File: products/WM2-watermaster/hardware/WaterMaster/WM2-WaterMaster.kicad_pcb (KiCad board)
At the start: 2 copper layers, 97.4 x 99.1 mm, 109 parts, among them J1 Flow_CONN, J12 Conn_01x04_Pin, J13 Conn_01x03_Pin, J2 Conn_Coaxial_Small, J3 PWR_CONN, J4 Conn_IN, J5 Conn_01x03_Pin, J7 Conn_RLY_EXTENDER, K1 Cube_Relay, K2 Cube_Relay, K3 Cube_Relay, K4 Cube_Relay, K5 Cube_Relay, K6 Cube_Relay, U1 ULN2003, U10 DS1307Z+, U13 AMS1117-5.0, U2 74HC595, U3 MT3608, U4 DS3231M, U5 ESP32 30 Pin CP2102 Developme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, U7 ISC-SX1262-B, U8 AP2112K-3.3, U9 74HC595, Y1 Crystal

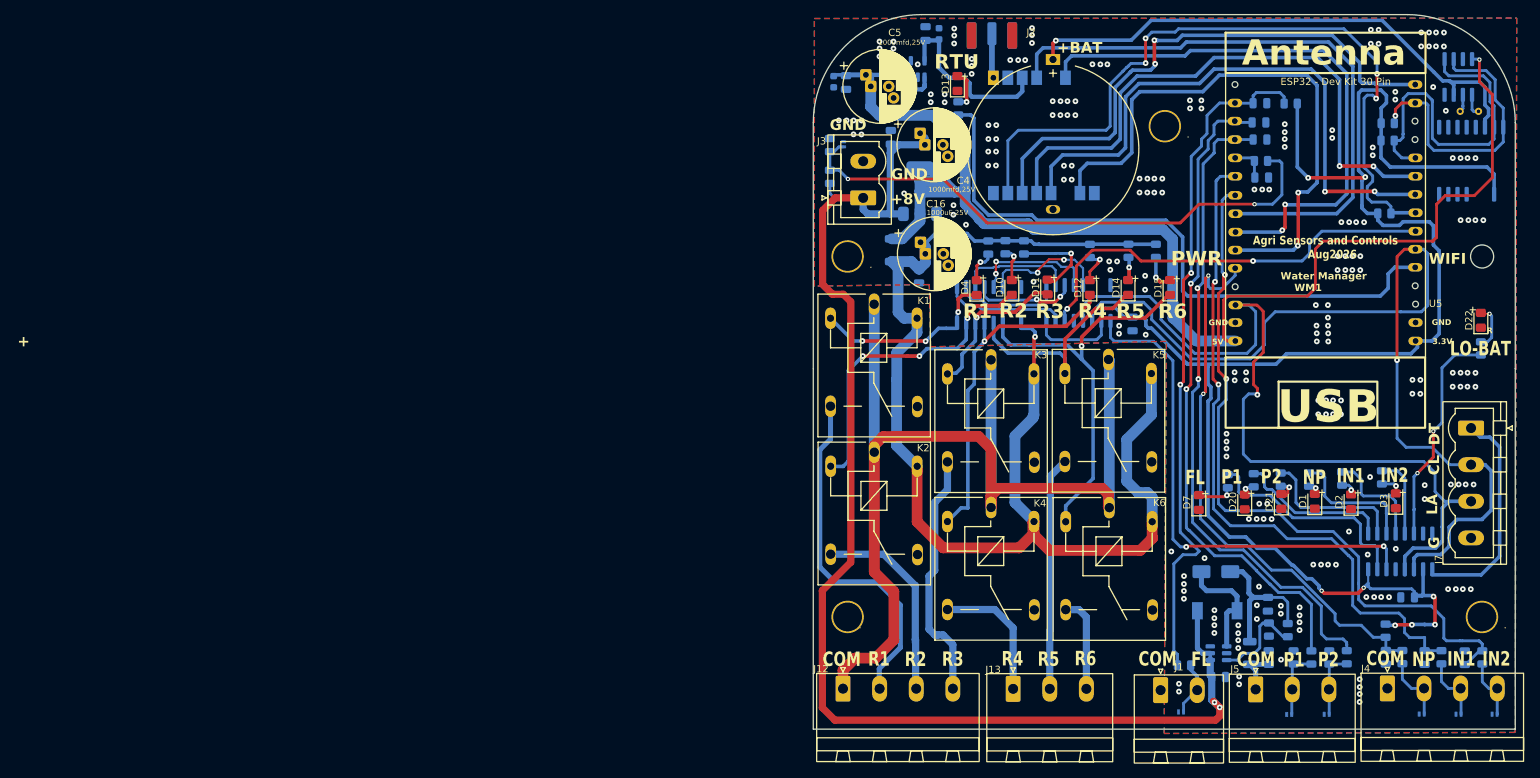
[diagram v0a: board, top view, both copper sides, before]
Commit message: Workshop labs page at /workshop, GPSIOAM workshop materials, pending WIP
- agrisense-webapp: public, no-login /workshop route (middleware allowlist +
  next.config.ts rewrite) serving the student labs page from public/workshop
- docs/workshops/gpsioam-2026: 4 Wokwi-ready ESP32 labs + Lab 4 reference
  solution, labs page template and build_site.py
- Pending work committed as-is: WM2 SolarNode/WaterMaster KiCad, WPC Pump
  Node Gerbers, FG1 flash tools, marketing video projects
- .gitignore: Next.js cache, *.tsbuildinfo, KiCad *.lck, .claude/settings.local.json;
  stop tracking .next/cache

Co-Authored-By: Claude Opus 5.5 <noreply@anthropic.com>
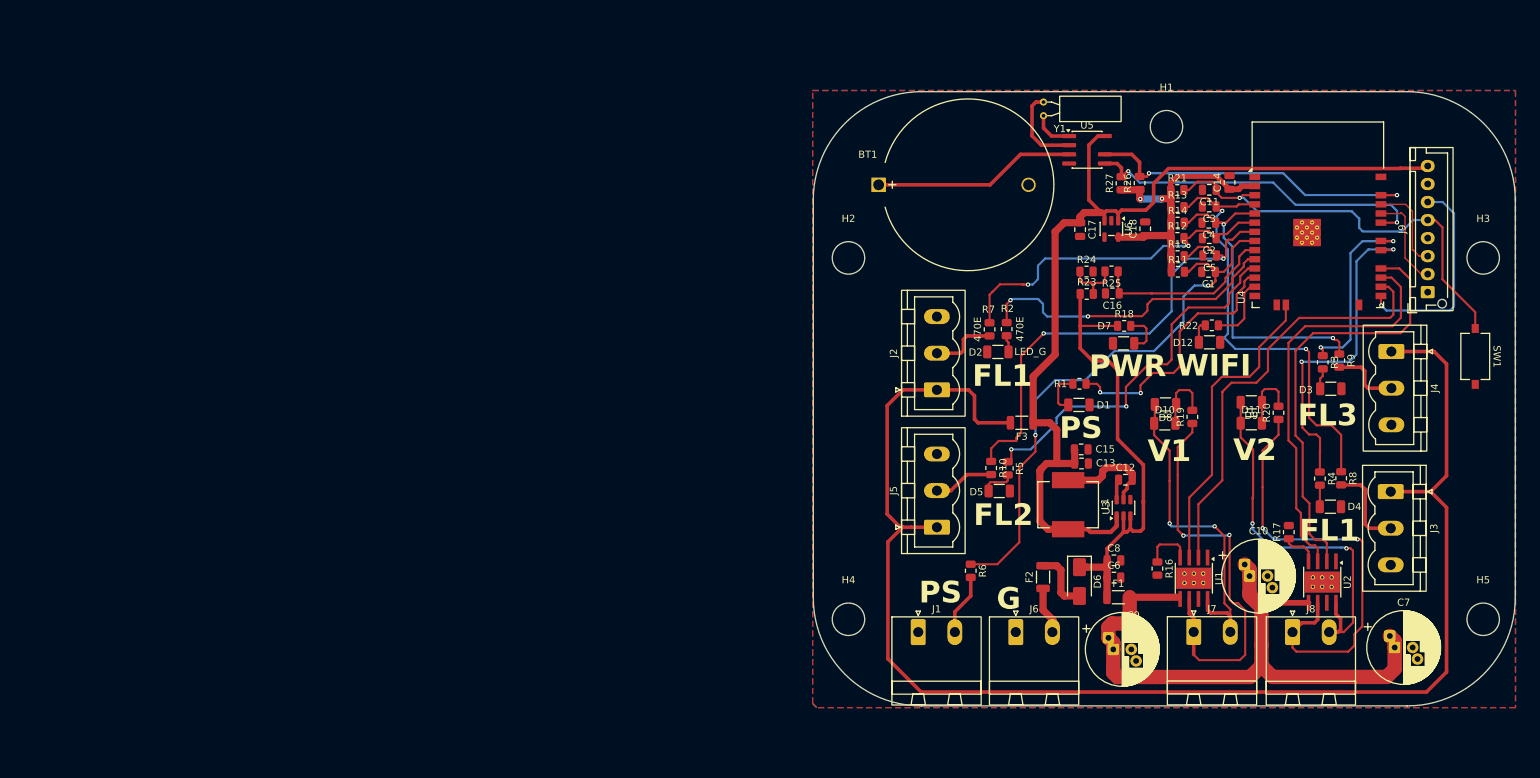
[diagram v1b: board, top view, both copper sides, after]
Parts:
- removed . (x5): MountingHole, MountingHole:MountingHole_3.2mm_M3
- removed C19: 100nF, Capacitor_SMD:C_0805_2012Metric
- removed C20, C21: 100pF, Capacitor_SMD:C_0805_2012Metric
- removed C22: 22µF, X7R, 35V,1210, Capacitor_SMD:C_0805_2012Metric
- removed D13: LED_Yellow_LoRa, LED_SMD:LED_0805_2012Metric_Pad1.15x1.40mm_HandSolder
- removed D14, D15: LED_YELLOW_PUMP, LED_SMD:LED_0805_2012Metric_Pad1.15x1.40mm_HandSolder
- removed D16, D17, D18, D19: PESD3V3U1UL, Diode_SMD:D_SOD-882
- removed D20: LED_Green_PR1, LED_SMD:LED_0805_2012Metric_Pad1.15x1.40mm_HandSolder
- removed D21: LED_Green_PR2, LED_SMD:LED_0805_2012Metric_Pad1.15x1.40mm_HandSolder
- removed D22: LED_R_LoBAT, LED_SMD:LED_0805_2012Metric_Pad1.15x1.40mm_HandSolder
- removed J12: Conn_01x04_Pin, Connector_Phoenix_MSTB:PhoenixContact_MSTBA_2,5_4-G-5,08_1x04_P5.08mm_Horizontal
- removed J13: Conn_01x03_Pin, Connector_Phoenix_MSTB:PhoenixContact_MSTBA_2,5_3-G-5,08_1x03_P5.08mm_Horizontal
- removed K1, K2, K3, K4, K5, K6: Cube_Relay, Relay_THT:Relay_SPDT_SANYOU_SRD_Series_Form_C
- removed R28, R29, R30, R31, R33: 470E, Resistor_SMD:R_0805_2012Metric
- removed R32: 10K, Resistor_SMD:R_0805_2012Metric
- removed U10: DS1307Z+, Package_SO:SOIC-8_3.9x4.9mm_P1.27mm
- removed U13: AMS1117-5.0, Package_TO_SOT_SMD:SOT-223-3_TabPin2
- removed U7: ISC-SX1262-B, RF_Module:Ai-Thinker-Ra-01-LoRa
- removed U8: AP2112K-3.3, Package_TO_SOT_SMD:SOT-23-5
- removed U9: 74HC595, Package_SO:SOIC-16_3.9x9.9mm_P1.27mm
- added C9: 1000mfd,25V, Capacitor_THT:CP_Radial_D10.0mm_P2.50mm_P5.00mm, F.Cu at (201.7, 114.5)
- added F3: Polyfuse_Small, Inductor_SMD:L_1206_3216Metric, F.Cu at (189.0, 83.1)
- added H1: MountingHole, MountingHole:MountingHole_4.5mm, F.Cu at (209.1, 42.0)
- added H2: MountingHole, MountingHole:MountingHole_4.5mm, F.Cu at (165.0, 60.2)
- added H3: MountingHole, MountingHole:MountingHole_4.5mm, F.Cu at (253.0, 60.2)
- added H4: MountingHole, MountingHole:MountingHole_4.5mm, F.Cu at (165.0, 110.3)
- added H5: MountingHole, MountingHole:MountingHole_4.5mm, F.Cu at (253.0, 110.3)
- added J6: SOLAR_12V_IN, Connector_Phoenix_MSTB:PhoenixContact_MSTBA_2,5_2-G-5,08_1x02_P5.08mm_Horizontal, F.Cu at (188.2, 112.1)
- added J8: LV_Conn, Connector_Phoenix_MSTB:PhoenixContact_MSTBA_2,5_2-G-5,08_1x02_P5.08mm_Horizontal, F.Cu at (226.6, 112.1)
- added J9: Programmer_Conn, Connector_JST:JST_XH_B8B-XH-AM_1x08_P2.50mm_Vertical, F.Cu at (245.3, 64.9)
- added R19: 470E, Resistor_SMD:R_0805_2012Metric, F.Cu at (212.7, 82.2)
- added SW1: RESET (EN), Button_Switch_SMD:SW_Tactile_SPST_NO_Straight_CK_PTS636Sx25SMTRLFS, F.Cu at (251.9, 73.9)
- added U6: AP2112K-3.3, Package_TO_SOT_SMD:SOT-23-5, F.Cu at (201.5, 56.2)
- C1, C2: value 100nF -> 100pF; moved to F.Cu
- C10: value 10mfd,10V tent -> 1000mfd,25V; footprint Capacitor_SMD:C_0603_1608Metric -> Capacitor_THT:CP_Radial_D10.0mm_P2.50mm_P5.00mm; moved to F.Cu
- C11, C3, C6, R1, R10, R12, R13, R2, R3, R4, R6, R8, R9: moved to F.Cu
- C12: value 10mfd,10V tentalum -> 100nF; footprint Capacitor_SMD:C_0603_1608Metric -> Capacitor_SMD:C_0805_2012Metric; moved to F.Cu
- C13, C15: value 100nF -> 22uF/16V; moved to F.Cu
- C14: value 22µF, X7R,35V,1210 -> 100nF; moved to F.Cu
- C16: value 1000uF,25V -> 100nF; footprint Capacitor_THT:CP_Radial_D10.0mm_P2.50mm_P5.00mm -> Capacitor_SMD:C_0805_2012Metric
- C17, C18: value 100nF -> 10mfd,10V tentalum; moved to F.Cu
- C4, C5: value 1000mfd,25V -> 100pF; footprint Capacitor_THT:CP_Radial_D10.0mm_P2.50mm_P5.00mm -> Capacitor_SMD:C_0805_2012Metric
- C7: value 100nF -> 1000mfd,25V; footprint Capacitor_SMD:C_0805_2012Metric -> Capacitor_THT:CP_Radial_D10.0mm_P2.50mm_P5.00mm; moved to F.Cu
- C8: value 100pF -> 10uF/25V; moved to F.Cu
- D1: value LED_GREEN_IN1 -> LED_GREEN_PS; footprint LED_SMD:LED_0805_2012Metric_Pad1.15x1.40mm_HandSolder -> Capacitor_SMD:C_1206_3216Metric
- D10: value LED_YELLOW_PUMP -> LED_V1_Yellow; footprint LED_SMD:LED_0805_2012Metric_Pad1.15x1.40mm_HandSolder -> Capacitor_SMD:C_1206_3216Metric
- D11: value LED_YELLOW_PUMP -> LED_V2_Yellow; footprint LED_SMD:LED_0805_2012Metric_Pad1.15x1.40mm_HandSolder -> Capacitor_SMD:C_1206_3216Metric
- D12: value LED_YELLOW_PUMP -> LED_B_WIFI; footprint LED_SMD:LED_0805_2012Metric_Pad1.15x1.40mm_HandSolder -> Capacitor_SMD:C_1206_3216Metric
- D2: value LED_GREEN_IN2 -> LED_Green_Flow; footprint LED_SMD:LED_0805_2012Metric_Pad1.15x1.40mm_HandSolder -> Capacitor_SMD:C_1206_3216Metric
- D3: value LED_GREEN_IN3 -> LED_Green_Flow; footprint LED_SMD:LED_0805_2012Metric_Pad1.15x1.40mm_HandSolder -> Capacitor_SMD:C_1206_3216Metric
- D4: value LED_YELLOW_PUMP -> LED_Green_Flow; footprint LED_SMD:LED_0805_2012Metric_Pad1.15x1.40mm_HandSolder -> Capacitor_SMD:C_1206_3216Metric
- D5: value PESD3V3U1UL -> LED_Green_Flow; footprint Diode_SMD:D_SOD-882 -> Capacitor_SMD:C_1206_3216Metric; moved to F.Cu
- D6: value PESD3V3U1UL -> SS34 (reverse-polarity); footprint Diode_SMD:D_SOD-882 -> Diode_SMD:D_SMA; moved to F.Cu
- D7: value LED_Green_Flow -> LED_G_PWR; footprint LED_SMD:LED_0805_2012Metric_Pad1.15x1.40mm_HandSolder -> Capacitor_SMD:C_1206_3216Metric
- D8: value PESD3V3U1UL -> LED_V1_Green; footprint Diode_SMD:D_SOD-882 -> Capacitor_SMD:C_1206_3216Metric; moved to F.Cu
- D9: value SS34 -> LED_V2_Green; footprint Diode_SMD:D_SMA -> Capacitor_SMD:C_1206_3216Metric; moved to F.Cu
- F1, F2: value Polyfuse_Small -> 500mA; moved to F.Cu
- J1: value Flow_CONN -> Press_Conn
- J2: value Conn_Coaxial_Small -> Flow_Conn; footprint Connector_Coaxial:SMA_Samtec_SMA-J-P-H-ST-EM1_EdgeMount -> Connector_Phoenix_MSTB:PhoenixContact_MSTBVA_2,5_3-G-5,08_1x03_P5.08mm_Vertical; moved to F.Cu
- J3: value PWR_CONN -> Flow_Conn; footprint Connector_Phoenix_MSTB:PhoenixContact_MSTBVA_2,5_2-G-5,08_1x02_P5.08mm_Vertical -> Connector_Phoenix_MSTB:PhoenixContact_MSTBVA_2,5_3-G-5,08_1x03_P5.08mm_Vertical
- J4: value Conn_IN -> Flow_Conn; footprint Connector_Phoenix_MSTB:PhoenixContact_MSTBA_2,5_4-G-5,08_1x04_P5.08mm_Horizontal -> Connector_Phoenix_MSTB:PhoenixContact_MSTBVA_2,5_3-G-5,08_1x03_P5.08mm_Vertical
- J5: value Conn_01x03_Pin -> Flow_Conn; footprint Connector_Phoenix_MSTB:PhoenixContact_MSTBA_2,5_3-G-5,08_1x03_P5.08mm_Horizontal -> Connector_Phoenix_MSTB:PhoenixContact_MSTBVA_2,5_3-G-5,08_1x03_P5.08mm_Vertical
- J7: value Conn_RLY_EXTENDER -> LV_Conn; footprint Connector_Phoenix_MSTB:PhoenixContact_MSTBVA_2,5_4-G-5,08_1x04_P5.08mm_Vertical -> Connector_Phoenix_MSTB:PhoenixContact_MSTBA_2,5_2-G-5,08_1x02_P5.08mm_Horizontal
- L1: value 10microH -> 4.7uH; footprint Inductor_SMD:L_6.3x6.3_H3 -> Inductor_SMD:L_Neosid_Ms85T; moved to F.Cu
- R11: value 470E -> 10K; moved to F.Cu
- R14: value 324K,1% -> 10K; moved to F.Cu
- R15: value 4K7 -> 10K; moved to F.Cu
- R16: value 4K7 -> 22K; moved to F.Cu
- R17: value 10K,1% -> 22K; moved to F.Cu
- R18: value 56.2K -> 470E; moved to F.Cu
- R20, R22, R25, R5: value 1K -> 470E; moved to F.Cu
- R21, R24: value 1K -> 10K; moved to F.Cu
- R23: value 470E -> 56.2K; moved to F.Cu
- R26, R27: value 150E,1% -> 4K7; moved to F.Cu
- R7: value 10K -> 470E; moved to F.Cu
- U1: value ULN2003 -> DRV8871DDA; footprint Package_SO:SOIC-16_3.9x9.9mm_P1.27mm -> Package_SO:Texas_HTSOP-8-1EP_3.9x4.9mm_P1.27mm_EP2.95x4.9mm_Mask2.4x3.1mm_ThermalVias; moved to F.Cu
- U2: value 74HC595 -> DRV8871DDA; footprint Package_SO:SOIC-16_3.9x9.9mm_P1.27mm -> Package_SO:Texas_HTSOP-8-1EP_3.9x4.9mm_P1.27mm_EP2.95x4.9mm_Mask2.4x3.1mm_ThermalVias; moved to F.Cu
- U3: value MT3608 -> AP63205WU (fixed 5.0V out); footprint Package_TO_SOT_SMD:SOT-23-6 -> Package_TO_SOT_SMD:TSOT-23-6; moved to F.Cu
- U4: value DS3231M -> ESP32-WROOM-32D; footprint Package_SO:SOIC-16W_7.5x10.3mm_P1.27mm -> RF_Module:ESP32-WROOM-32D; moved to F.Cu
- U5: value ESP32 30 Pin CP2102 Development Board -> DS1307Z+; footprint PCM_Espressif:ESP32-C3-DevKitM-1 -> Package_SO:SOIC-8_3.9x4.9mm_P1.27mm
- Y1: footprint Crystal:Crystal_AT310_D3.0mm_L10.0mm_Horizontal -> Crystal:Crystal_C38-LF_D3.0mm_L8.0mm_Horizontal; moved to F.Cu
- moved C7 109.2 mm to (240.8, 114.2), turned to 0 degrees
- moved C10 89.6 mm to (220.6, 104.3), turned to 0 degrees
- moved J3 83.8 mm to (240.2, 92.6), turned to -90 degrees
- moved R26 70.9 mm to (205.4, 49.8)
- moved R27 70.0 mm to (202.9, 49.8)
- moved R10 69.9 mm to (184.8, 89.3), turned to -90 degrees
- moved R7 69.0 mm to (184.6, 70.1)
- moved C14 68.6 mm to (217.8, 49.7), turned to 90 degrees
- moved C6 68.5 mm to (201.8, 104.5), turned to 0 degrees
- moved C17 68.3 mm to (197.1, 56.3), turned to -90 degrees
- moved R16 67.4 mm to (207.8, 103.3), turned to -90 degrees
- moved C3 67.1 mm to (215.0, 53.1), turned to 180 degrees
- moved C12 67.0 mm to (203.4, 91.0), turned to 0 degrees
- moved C8 66.6 mm to (201.8, 102.1)
- moved D5 66.3 mm to (185.9, 92.5)
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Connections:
- C1 pad 1: /IN3 -> /PS_MCU
- C10 pad 1: +5V -> +12V_LV
- C11 pad 1: +3.3V -> /EN
- C12 pad 1: +3.3VL -> Net-(U3-BST)
- C12 pad 2: GND -> Net-(U3-SW)
- C13 pad 1: +3.3VL -> +5V
- C14 pad 1: +8V -> +3.3V
- C15 pad 1: +5VR -> +5V
- C16 pad 1: +5VR -> /Batt_Mon
- C17 pad 1: +3.3V -> +5V
- C18 pad 1: +20VPR -> +3.3V
- C2 pad 1: /IN2 -> /Flow_MCU1
- C3 pad 1: /IN1 -> /Flow_MCU3
- C4 pad 1: +8V -> /Flow_MCU4
- C5 pad 1: +5V -> /Flow_MCU2
- C6 pad 1: +8V -> +12V
- C7 pad 1: +5V -> +12V_LV
- C8 pad 1: /Flow_MCU -> +12V
- D10 pad 1: /RELAY2_COIL -> /V1_OUT2
- D11 pad 1: /RELAY3_COIL -> /V2_OUT2
- D12 pad 1: /RELAY4_COIL -> GND
- D4 pad 1: /RELAY1_COIL -> GND
- D5 pad 1: /IN1_CON -> GND
- D5 pad 2: GND -> Net-(D5-A)
- D6 pad 1: /IN2_CON -> +12V
- D6 pad 2: GND -> Net-(D6-A)
- D8 pad 1: /Flow_CON -> Net-(D10-A)
- D8 pad 2: GND -> /V1_OUT2
- D9 pad 1: +20V -> Net-(D11-A)
- D9 pad 2: Net-(D9-A) -> /V2_OUT2
- F1 pad 1: +20V -> +12V
- F1 pad 2: +20VPR -> +12V_LV
- F2 pad 1: +5V -> Net-(J6-Pin_2)
- F2 pad 2: +5VR -> Net-(D6-A)
- J1 pad 2: /Flow_CON -> Net-(J1-Pin_2)
- J2 pad 1: Net-(J2-In) -> +5V_Ext
- J2 pad 2: GND -> Net-(J2-Pin_2)
- J3 pad 1: +8V -> +5V_Ext
- J3 pad 2: GND -> Net-(J3-Pin_2)
- J4 pad 1: GND -> +5V_Ext
- J4 pad 2: /IN1_CON -> Net-(J4-Pin_2)
- J4 pad 3: /IN2_CON -> GND
- J5 pad 1: +20VPR -> +5V_Ext
- J5 pad 2: /Press_IN1_CON -> Net-(J5-Pin_2)
- J5 pad 3: /Press_IN2_CON -> GND
- J7 pad 1: /RLY_DATA_EXT -> /V1_OUT1
- J7 pad 2: /RLY_CLK -> /V1_OUT2
- L1 pad 1: +8V -> Net-(U3-SW)
- L1 pad 2: Net-(D9-A) -> +5V
- R1 pad 1: /IN3_LED -> /PS_LED
- R1 pad 2: Net-(D3-A) -> Net-(D1-A)
- R10 pad 1: /LOBATT_LED -> /Flow_MCU2
- R10 pad 2: Net-(D22-A) -> Net-(J5-Pin_2)
- R11 pad 1: /Flow_MCU -> +3.3V
- R11 pad 2: /Flow_CON -> /PS_MCU
- R12 pad 2: /Flow_MCU -> /Flow_MCU1
- R13 pad 2: /NSS -> /Flow_MCU3
- R14 pad 1: +20V -> +3.3V
- R14 pad 2: Net-(U3-FB) -> /Flow_MCU4
- R15 pad 2: /SCL -> /Flow_MCU2
- R16 pad 1: +3.3V -> Net-(U1-ILIM)
- R16 pad 2: /SDA -> GND
- R17 pad 1: Net-(U3-FB) -> Net-(U2-ILIM)
- R18 pad 1: +8V -> +12V
- R18 pad 2: Net-(D16-K) -> Net-(D7-A)
- R2 pad 1: /IN2_LED -> /Flow_LED1
- R20 pad 1: +5VR -> /V2_OUT1
- R20 pad 2: Net-(D10-A) -> Net-(D11-A)
- R21 pad 1: +5VR -> +3.3V
- R21 pad 2: Net-(D11-A) -> /EN
- R22 pad 1: +5VR -> /WIFI_LED
- R23 pad 1: /LoRa_LED -> +12V
- R23 pad 2: Net-(D13-A) -> Net-(R23-Pad2)
- R24 pad 1: +5VR -> Net-(R23-Pad2)
- R24 pad 2: Net-(D14-A) -> GND
- R25 pad 1: +5VR -> /Batt_Mon
- R25 pad 2: Net-(D15-A) -> Net-(R23-Pad2)
- R26 pad 1: /Press_IN2_CON -> +3.3V
- R26 pad 2: GND -> /SCL
- R27 pad 1: /Press_IN1_CON -> +3.3V
- R27 pad 2: GND -> /SDA
- R3 pad 1: /IN3 -> /Flow_LED3
- R3 pad 2: /IN3_CON -> Net-(D3-A)
- R4 pad 1: /IN2 -> /Flow_LED4
- R4 pad 2: /IN2_CON -> Net-(D4-A)
- R5 pad 1: +5VR -> /Flow_LED2
- R5 pad 2: Net-(D4-A) -> Net-(D5-A)
- R6 pad 1: /Flow_LED -> /PS_MCU
- R6 pad 2: Net-(D7-A) -> Net-(J1-Pin_2)
- R7 pad 1: +3.3V -> /Flow_MCU1
- R7 pad 2: /IN1 -> Net-(J2-Pin_2)
- R8 pad 1: /IN1_LED -> /Flow_MCU3
- R8 pad 2: Net-(D1-A) -> Net-(J3-Pin_2)
- R9 pad 1: /IN1 -> /Flow_MCU4
- R9 pad 2: /IN1_CON -> Net-(J4-Pin_2)
- U1 pad 1: /RELAY1_MCU -> GND
- U1 pad 2: /RELAY2_MCU -> /LV1_IN2_MCU
- U1 pad 3: /RELAY3_MCU -> /LV1_IN1_MCU
- U1 pad 4: /RELAY4_MCU -> Net-(U1-ILIM)
- U1 pad 5: /RELAY5_MCU -> +12V_LV
- U1 pad 6: /RELAY6_MCU -> /V1_OUT1
- U1 pad 8: GND -> /V1_OUT2
- U1 pad 9: +5VR -> GND
- U2 pad 1: /RELAY2_MCU -> GND
- U2 pad 2: /RELAY3_MCU -> /LV2_IN2_MCU
- U2 pad 3: /RELAY4_MCU -> /LV2_IN1_MCU
- U2 pad 4: /RELAY5_MCU -> Net-(U2-ILIM)
- U2 pad 5: /RELAY6_MCU -> +12V_LV
- U2 pad 8: GND -> /V2_OUT2
- U2 pad 9: /RLY_DATA_OUT -> GND
- U3 pad 1: Net-(D9-A) -> +5V
- U3 pad 2: GND -> +12V
- U3 pad 3: Net-(U3-FB) -> +12V
- U3 pad 4: +8V -> GND
- U3 pad 5: +8V -> Net-(U3-SW)
- U3 pad 6: unconnected-(U3-NC-Pad6) -> Net-(U3-BST)
- U4 pad 10: GND -> /Flow_LED1
- U4 pad 11: GND -> /Flow_LED2
- U4 pad 12: GND -> /PS_LED
- U4 pad 13: GND -> /WIFI_LED
- U4 pad 14: /BATT -> unconnected-(U4-IO12-Pad14)
- U4 pad 15: /SDA -> GND
- U4 pad 16: /SCL -> /LV1_IN1_MCU
- U4 pad 5: GND -> /Flow_MCU4
- U4 pad 6: GND -> /Flow_MCU1
- U4 pad 7: GND -> /Flow_MCU2
- U4 pad 8: GND -> /PS_MCU
- U4 pad 9: GND -> /Batt_Mon
- U5 pad 1: +3.3V -> Net-(U5-X1)
- U5 pad 2: GND -> Net-(U5-X2)
- U5 pad 5: /LoRa_LED -> /SDA
- U5 pad 6: /RLY_CLK -> /SCL
- U5 pad 8: /NSS -> +5V
- Y1 pad 1: Net-(U10-X1) -> Net-(U5-X1)
- Y1 pad 2: Net-(U10-X2) -> Net-(U5-X2)
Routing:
- net +5V_Ext: track 0.00 -> 202.6 mm
- net +3.3V: track 236.8 -> 41.0 mm, vias 8 -> 2
- net +8V: track 183.9 -> 0.00 mm, vias 2 -> 0
- net +5VR: track 180.7 -> 0.00 mm, vias 1 -> 0
- net /RLY_COMM: track 147.2 -> 0.00 mm
- net /RLY_CLK: track 133.6 -> 0.00 mm, vias 1 -> 0
- net /RLY_LATCH: track 119.7 -> 0.00 mm, vias 1 -> 0
- net /NSS: track 101.7 -> 0.00 mm, vias 4 -> 0
- net /IN3: track 100.0 -> 0.00 mm, vias 2 -> 0
- net /Flow_MCU: track 95.5 -> 0.00 mm, vias 2 -> 0
- net /IN2: track 94.9 -> 0.00 mm, vias 2 -> 0
- net /Press_IN1_MCU: track 91.3 -> 0.00 mm, vias 2 -> 0
- net /Press_IN2_MCU: track 91.3 -> 0.00 mm, vias 2 -> 0
- net +12V_LV: track 0.00 -> 91.2 mm
- net /LoRa_LED: track 87.7 -> 0.00 mm
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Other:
- board size 97.4 x 99.1 mm -> 97.4 x 85.2 mm
- board text added: "F1"
- board text added: "F2"
- board text added: "F3"
- board text added: "F4"
- board text added: "FL1"
- board text added: "FL2"
- board text added: "FL3"
- board text added: "LED_G"
- board text added: "PS"
- board text added: "V1"
- board text added: "V2"
- board text removed: "+"
- board text removed: "+8V"
- board text removed: "+BAT"
- board text removed: "1"
- board text removed: "3.3V"
- board text removed: "5V"
- board text removed: "Agri Sensors and Controls Aug2026"
- board text removed: "CL"
- board text removed: "COM"
- board text removed: "DT"
- board text removed: "FL"
- board text removed: "GND"
- board text removed: "IN1"
- board text removed: "IN2"
- board text removed: "LA"
- board text removed: "LO-BAT"
- board text removed: "NP"
- board text removed: "P1"
- board text removed: "P2"
- board text removed: "R"
- board text removed: "R1"
- board text removed: "R2"
- board text removed: "R3"
- board text removed: "R4"
- board text removed: "R5"
- board text removed: "R6"
- board text removed: "RTU"
- board text removed: "Water Manager WM1"

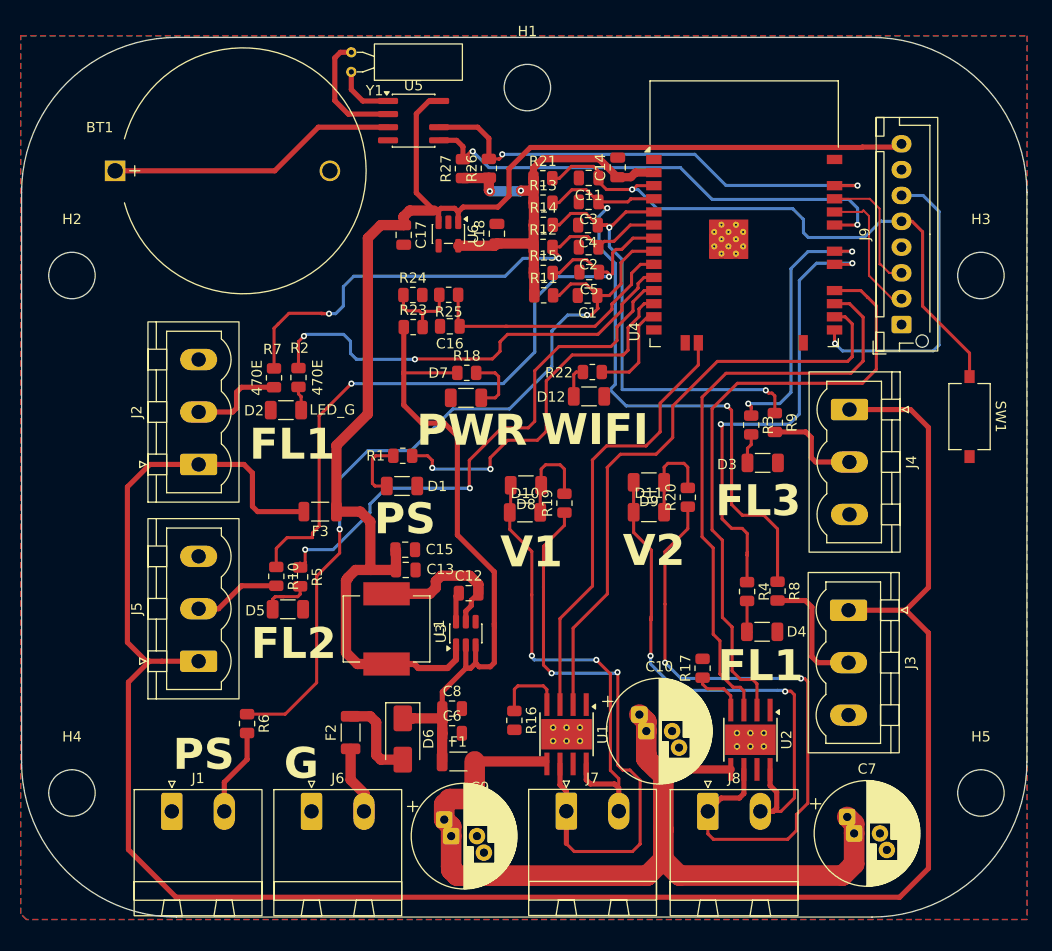
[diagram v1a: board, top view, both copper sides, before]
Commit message: WM2-WaterMaster: redesign for Girish Farm (ESP32-WROOM-32D, solar/battery)
Full schematic redesign of the WM2 main board, moving from the WM1-
copied ESP32-C3 devkit design to a bare ESP32-WROOM-32D module for
the extra GPIO headroom this deployment needs:

- 12V solar input -> AP63205WU buck (5V) -> AP2112K-3.3 LDO (3.3V)
- 4x flow sensor + 1x pressure switch inputs, each with a firmware-
  driven LED (stretched blink) on its own GPIO for field troubleshooting
- Battery voltage monitoring (resistor divider -> ADC)
- WiFi status LED
- 2x latch-valve driver (DRV8871) with anti-parallel LED pairs across
  OUT1/OUT2, catching both open and close pulses without spending a
  GPIO on it
- 2x relay-based valve control as an alternate/either-or population
  option, sharing the same MCU control nets as the latch drivers
- DS1307Z+ RTC with CR2032 backup
- 8-pin bare UART header (no onboard USB-UART chip) for one-time
  factory flashing via an external CP2102-based programmer with
  auto-reset (EN/IO0 driven by the programmer's own transistor
  circuit); all further updates go out over WiFi OTA

Also includes the first full PCB layout and regenerated gerbers/
production zip (WM2-Girish.zip, replacing the placeholder mini zip).

Co-Authored-By: Claude Sonnet 5 <noreply@anthropic.com>
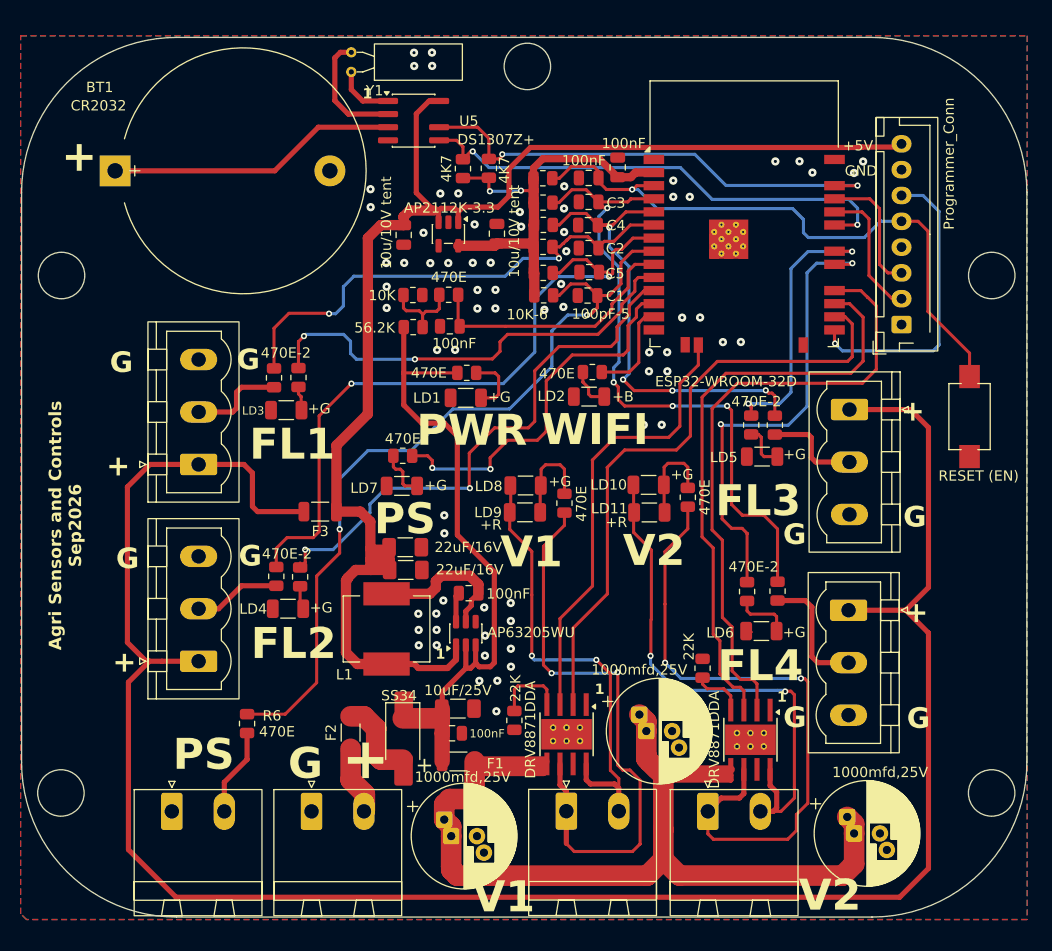
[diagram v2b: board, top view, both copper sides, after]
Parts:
- removed D1: LED_GREEN_PS, Capacitor_SMD:C_1206_3216Metric
- removed D10: LED_V1_Yellow, Capacitor_SMD:C_1206_3216Metric
- removed D11: LED_V2_Yellow, Capacitor_SMD:C_1206_3216Metric
- removed D12: LED_B_WIFI, Capacitor_SMD:C_1206_3216Metric
- removed D2, D3, D4, D5: LED_Green_Flow, Capacitor_SMD:C_1206_3216Metric
- removed D7: LED_G_PWR, Capacitor_SMD:C_1206_3216Metric
- removed D8: LED_V1_Green, Capacitor_SMD:C_1206_3216Metric
- removed D9: LED_V2_Green, Capacitor_SMD:C_1206_3216Metric
- added LD1: LED_G_PWR, Capacitor_SMD:C_1206_3216Metric, F.Cu at (203.1, 72.0)
- added LD10: LED_V2_Green, Capacitor_SMD:C_1206_3216Metric, F.Cu at (220.8, 80.5)
- added LD11: LED_V2_Yellow, Capacitor_SMD:C_1206_3216Metric, F.Cu at (220.9, 83.1)
- added LD2: LED_B_WIFI, Capacitor_SMD:C_1206_3216Metric, F.Cu at (215.1, 71.9)
- added LD3: LED_Green_Flow, Capacitor_SMD:C_1206_3216Metric, F.Cu at (185.7, 73.2)
- added LD4: LED_Green_Flow, Capacitor_SMD:C_1206_3216Metric, F.Cu at (185.9, 92.5)
- added LD5: LED_Green_Flow, Capacitor_SMD:C_1206_3216Metric, F.Cu at (231.8, 77.7)
- added LD6: LED_Green_Flow, Capacitor_SMD:C_1206_3216Metric, F.Cu at (231.8, 94.6)
- added LD7: LED_GREEN_PS, Capacitor_SMD:C_1206_3216Metric, F.Cu at (196.9, 80.6)
- added LD8: LED_V1_Green, Capacitor_SMD:C_1206_3216Metric, F.Cu at (208.9, 80.5)
- added LD9: LED_V1_Yellow, Capacitor_SMD:C_1206_3216Metric, F.Cu at (208.9, 83.1)
- C13, C15, C8: footprint Capacitor_SMD:C_0805_2012Metric -> Capacitor_SMD:C_1206_3216Metric_Pad1.33x1.80mm_HandSolder
- C17, C18: value 10mfd,10V tentalum -> 10u/10V tent
- D6: value SS34 (reverse-polarity) -> SS34
- U3: value AP63205WU (fixed 5.0V out) -> AP63205WU
- moved H1 2.05 mm to (209.1, 39.9)
- moved H4 1.07 mm to (163.9, 110.3)
- moved H3 1.05 mm to (254.1, 60.2)
- moved H5 1.04 mm to (254.1, 110.3)
- moved H2 1.01 mm to (164.0, 60.2)
- moved C8 0.56 mm to (202.4, 102.1)
- moved R9 0.25 mm to (233.1, 74.7)
- moved C15 0.24 mm to (197.3, 86.5)
- moved C2 0.08 mm to (215.0, 57.5)
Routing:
- net +5V: track 136.1 -> 141.0 mm
- net Net-(LD4-A): track 4.93 -> 2.30 mm
- net /V2_OUT1: track 65.6 -> 63.3 mm
- net Net-(LD6-A): track 3.65 -> 5.45 mm
- net Net-(LD5-A): track 2.91 -> 4.37 mm
- net Net-(LD7-A): track 6.02 -> 4.83 mm
- net Net-(J1-Pin_2): track 9.66 -> 8.50 mm
- net /LV1_IN2_MCU: track 59.5 -> 60.4 mm
- net Net-(LD2-A): track 3.11 -> 3.99 mm
- net /LV1_IN1_MCU: track 42.9 -> 43.7 mm
- net GND: track 0.25 -> 0.94 mm, vias 0 -> 70
- net /Flow_MCU4: track 45.4 -> 45.6 mm, vias 2 -> 4
- net /Flow_MCU3: track 63.1 -> 63.2 mm, vias 2 -> 4
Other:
- board text added: "+"
- board text added: "+5V"
- board text added: "+B"
- board text added: "+G"
- board text added: "+R"
- board text added: "1"
- board text added: "100pF-5"
- board text added: "10K-6"
- board text added: "470E-2"
- board text added: "Agri Sensors and Controls Sep2026"
- board text added: "FL4"
- board text added: "GND"
- board text removed: "F1"
- board text removed: "F2"
- board text removed: "F3"
- board text removed: "F4"
- board text removed: "LED_G"

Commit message: WM2 WaterMaster: updated PCB and GERBER-FLOW fab set
Co-Authored-By: Claude Opus 5.5 <noreply@anthropic.com>
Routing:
- net /EN: track 60.3 -> 62.6 mm
- net /Flow_LED4: track 45.7 -> 44.3 mm
- net /Flow_LED3: track 26.2 -> 25.4 mm
- net GND: vias 70 -> 73
